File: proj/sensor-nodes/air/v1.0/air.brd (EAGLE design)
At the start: 73 parts, among them J1 54602-908LF, J2 54602-908LF, U2 PCA9615DPJ, U3 MIC4680YM-TR, U4 LM2937IMP3.3NOPB, U5 SHT25, U6 CCS811, U7 T6713-5K, U8 HPP845E034R5

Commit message: minor changes to air sensor node after design review
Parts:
- removed L2: 68uH, openag-inductors:UP2B
- removed SJ4: (no value), openag-connectors:SOLDERJUMPER_REFLOW_NOPASTE
- removed TP10, TP11, TP12, TP31: TPTP06R, openag-testpads:TP06R
- added L1: 68uH, openag-inductors:UP2B
- added SJ2: (no value), openag-connectors:SOLDERJUMPER_REFLOW_NOPASTE
- added TP5, TP6, TP7: TPTP06R, openag-testpads:TP06R
- C4: device openag-capacitors:CT7343 -> openag-capacitors:C0805
- D4: value B260A-13-F -> SBR2A40P1-7; device openag-diodes:SMA -> openag-diodes:POWERDI123
- moved FRAME1 24.1 mm to (77.2, 3.30), turned to 0 degrees
- moved C2\1 22.9 mm to (107.2, 36.1)
- moved C8 22.9 mm to (110.7, 43.1)
- moved R18 22.9 mm to (105.3, 43.1)
- moved TP13 22.9 mm to (111.3, 33.5)
- moved TP14 22.9 mm to (110.0, 33.5)
- moved TP15 22.9 mm to (105.4, 45.0)
- moved TP16 22.9 mm to (103.4, 33.5)
- moved U6 22.9 mm to (109.2, 39.4)
- moved TP24 19.0 mm to (86.6, 45.0), turned to 90 degrees
- moved TP17 17.7 mm to (79.2, 35.1), turned to 90 degrees
- moved TP18 16.8 mm to (78.2, 34.8), turned to 90 degrees
- moved TP23 16.0 mm to (84.6, 36.1), turned to 90 degrees
- moved C10 15.0 mm to (88.9, 42.9), turned to 0 degrees
- moved TP20 13.0 mm to (74.2, 34.8), turned to 90 degrees
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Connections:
- removed net TAB: U4.4
- net +24V: now also C4.1, TP7.TP; no longer C4.+, TP12.TP
- net +5V: now also SJ2.2, TP5.TP; no longer SJ4.2, TP10.TP
- net GND: now also C4.2, D4.-, TP6.TP, U4.4; no longer C4.-, D4.2, TP11.TP, TP31.TP
- net N$31: now also D4.+, L1.1; no longer D4.1, L2.1
- net N$33: now also L1.2, SJ2.1; no longer L2.2, SJ4.1
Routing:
- net +3V3: track 343.5 -> 361.8 mm, vias 2 -> 4
- net N$33: track 25.9 -> 10.7 mm, vias 0 -> 2
- net N$31: track 27.3 -> 16.2 mm, vias 0 -> 2
- net SDA: track 130.4 -> 138.5 mm
- net SCL: track 131.4 -> 137.6 mm, vias 6 -> 4
- net +5V: track 162.2 -> 163.7 mm
- net +24V: track 50.5 -> 51.1 mm
- net GND: vias 9 -> 41
- added copper zone on layer 1, net N$31
- added copper zone on layer 16, net N$31
- added copper zone on layer 1, net N$33
- added copper zone on layer 16, net N$33
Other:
- board outline added: 116.8 x 54.6 mm
- board text added: "24V-to-5V@1A Switching Regulator w/Indicator LED + Enable"
- board text added: "NC"
- board text removed: "24V to 5V@1A Switching Regulator w/Indicator LED + Enable"

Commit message: added light and rj12 nodes, started working on light controller v2
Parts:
- R13, R15, R16, R17: value NV -> 600
- R14, R19: value NV -> 120
- R2, R7: value 100 OHM -> 100
- R20, R21: value NV -> 10K
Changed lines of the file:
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@@
 <setting verticaltext="up"/>
 </settings>
-<grid distance="10" unitdist="mil" unit="mil" style="lines" multiple="1" display="yes" altdistance="5" altunitdist="mil" altunit="mil"/>
+<grid distance="50" unitdist="mil" unit="mil" style="lines" multiple="1" display="yes" altdistance="5" altunitdist="mil" altunit="mil"/>
 <layers>
 <layer number="1" name="Top" color="4" fill="1" visible="yes" active="yes"/>
@@
 <attribute name="VERIFIED" value="NO" x="52.451" y="36.957" size="1.778" layer="27" rot="R180" display="off"/>
 </element>
-<element name="R2" library="openag-resistors" package="RC0603N" value="100 OHM" x="52.451" y="41.148" smashed="yes" rot="R90">
+<element name="R2" library="openag-resistors" package="RC0603N" value="100" x="52.451" y="41.148" smashed="yes" rot="R90">
 <attribute name="NAME" x="51.9557" y="42.4815" size="0.762" layer="25" ratio="6" rot="SR0"/>
 <attribute name="POPULATE" value="YES" x="52.451" y="41.148" size="1.778" layer="27" rot="R90" display="off"/>
@@
 <attribute name="VALUE" value="PCA9615DPJ" x="29.337" y="17.272" size="1.778" layer="27" rot="R270" display="off"/>
 </element>
-<element name="R13" library="openag-resistors" package="RC0603N" value="NV" x="32.639" y="18.288" smashed="yes" rot="R90">
+<element name="R13" library="openag-resistors" package="RC0603N" value="600" x="32.639" y="18.288" smashed="yes" rot="R90">
 <attribute name="NAME" x="34.036" y="17.653" size="0.762" layer="25" rot="R90"/>
-<attribute name="VALUE" value="NV" x="32.004" y="17.653" size="0.762" layer="27" rot="R90"/>
-</element>
-<element name="R14" library="openag-resistors" package="RC0603N" value="NV" x="32.639" y="15.24" smashed="yes" rot="R90">
+<attribute name="VALUE" value="600" x="32.004" y="17.653" size="0.762" layer="27" rot="R90"/>
+</element>
+<element name="R14" library="openag-resistors" package="RC0603N" value="120" x="32.639" y="15.24" smashed="yes" rot="R90">
 <attribute name="NAME" x="34.036" y="14.605" size="0.762" layer="25" rot="R90"/>
-<attribute name="VALUE" value="NV" x="32.004" y="14.605" size="0.762" layer="27" rot="R90"/>
-</element>
-<element name="R15" library="openag-resistors" package="RC0603N" value="NV" x="32.639" y="12.192" smashed="yes" rot="R90">
+<attribute name="VALUE" value="120" x="32.004" y="14.605" size="0.762" layer="27" rot="R90"/>
+</element>
+<element name="R15" library="openag-resistors" package="RC0603N" value="600" x="32.639" y="12.192" smashed="yes" rot="R90">
 <attribute name="NAME" x="34.036" y="11.557" size="0.762" layer="25" rot="R90"/>
-<attribute name="VALUE" value="NV" x="32.004" y="11.557" size="0.762" layer="27" rot="R90"/>
-</element>
-<element name="R16" library="openag-resistors" package="RC0603N" value="NV" x="30.099" y="11.684" smashed="yes">
+<attribute name="VALUE" value="600" x="32.004" y="11.557" size="0.762" layer="27" rot="R90"/>
+</element>
+<element name="R16" library="openag-resistors" package="RC0603N" value="600" x="30.099" y="11.684" smashed="yes">
 <attribute name="NAME" x="30.734" y="11.049" size="0.762" layer="25" rot="R180"/>
-<attribute name="VALUE" value="NV" x="30.734" y="13.081" size="0.762" layer="27" rot="R180"/>
-</element>
-<element name="R17" library="openag-resistors" package="RC0603N" value="NV" x="26.162" y="14.224" smashed="yes" rot="R270">
+<attribute name="VALUE" value="600" x="30.734" y="13.081" size="0.762" layer="27" rot="R180"/>
+</element>
+<element name="R17" library="openag-resistors" package="RC0603N" value="600" x="26.162" y="14.224" smashed="yes" rot="R270">
 <attribute name="NAME" x="25.527" y="13.589" size="0.762" layer="25" rot="R90"/>
-<attribute name="VALUE" value="NV" x="27.559" y="13.589" size="0.762" layer="27" rot="R90"/>
-</element>
-<element name="R19" library="openag-resistors" package="RC0603N" value="NV" x="27.051" y="11.684" smashed="yes">
+<attribute name="VALUE" value="600" x="27.559" y="13.589" size="0.762" layer="27" rot="R90"/>
+</element>
+<element name="R19" library="openag-resistors" package="RC0603N" value="120" x="27.051" y="11.684" smashed="yes">
 <attribute name="NAME" x="27.432" y="11.049" size="0.762" layer="25" rot="R180"/>
-<attribute name="VALUE" value="NV" x="27.686" y="13.081" size="0.762" layer="27" rot="R180"/>
-</element>
-<element name="R20" library="openag-resistors" package="RC0603N" value="NV" x="29.718" y="22.225" smashed="yes">
+<attribute name="VALUE" value="120" x="27.686" y="13.081" size="0.762" layer="27" rot="R180"/>
+</element>
+<element name="R20" library="openag-resistors" package="RC0603N" value="10K" x="29.718" y="22.225" smashed="yes">
 <attribute name="NAME" x="28.448" y="21.717" size="0.762" layer="25" rot="R90"/>
-<attribute name="VALUE" value="NV" x="31.75" y="21.463" size="0.762" layer="27" rot="R90"/>
-</element>
-<element name="R21" library="openag-resistors" package="RC0603N" value="NV" x="29.718" y="25.019" smashed="yes">
+<attribute name="POPULATE" value="YES" x="29.718" y="22.225" size="1.778" layer="27" display="off"/>
+<attribute name="VALUE" value="10K" x="31.75" y="21.463" size="0.762" layer="27" rot="R90"/>
+<attribute name="VERIFIED" value="NO" x="29.718" y="22.225" size="1.778" layer="27" display="off"/>
+</element>
+<element name="R21" library="openag-resistors" package="RC0603N" value="10K" x="29.718" y="25.019" smashed="yes">
 <attribute name="NAME" x="28.448" y="24.257" size="0.762" layer="25" rot="R90"/>
-<attribute name="VALUE" value="NV" x="31.75" y="24.257" size="0.762" layer="27" rot="R90"/>
+<attribute name="POPULATE" value="YES" x="29.718" y="25.019" size="1.778" layer="27" display="off"/>
+<attribute name="VALUE" value="10K" x="31.75" y="24.257" size="0.762" layer="27" rot="R90"/>
+<attribute name="VERIFIED" value="NO" x="29.718" y="25.019" size="1.778" layer="27" display="off"/>
 </element>
 <element name="J2" library="openag_connector" package="OPENAG-V1-RJ45" value="54602-908LF" x="13.97" y="35.56" smashed="yes" rot="R270">
@@
 <attribute name="VALUE" value="976 Ohm" x="48.26" y="24.892" size="0.762" layer="27" ratio="6" rot="R270"/>
 </element>
-<element name="R7" library="openag-resistors" package="RC0603N" value="100 OHM" x="53.213" y="18.288" smashed="yes" rot="R180">
+<element name="R7" library="openag-resistors" package="RC0603N" value="100" x="53.213" y="18.288" smashed="yes" rot="R180">
 <attribute name="NAME" x="52.9082" y="18.9865" size="0.762" layer="25" ratio="6" rot="SR0"/>
 <attribute name="POPULATE" value="YES" x="53.213" y="18.288" size="1.778" layer="27" rot="R180" display="off"/>
-<attribute name="VALUE" x="54.229" y="17.78" size="0.3556" layer="27" ratio="6" rot="R180"/>
+<attribute name="VALUE" value="100" x="54.229" y="17.78" size="0.3556" layer="27" ratio="6" rot="R180"/>
 <attribute name="VERIFIED" value="NO" x="53.213" y="18.288" size="1.778" layer="27" rot="R180" display="off"/>
 </element>

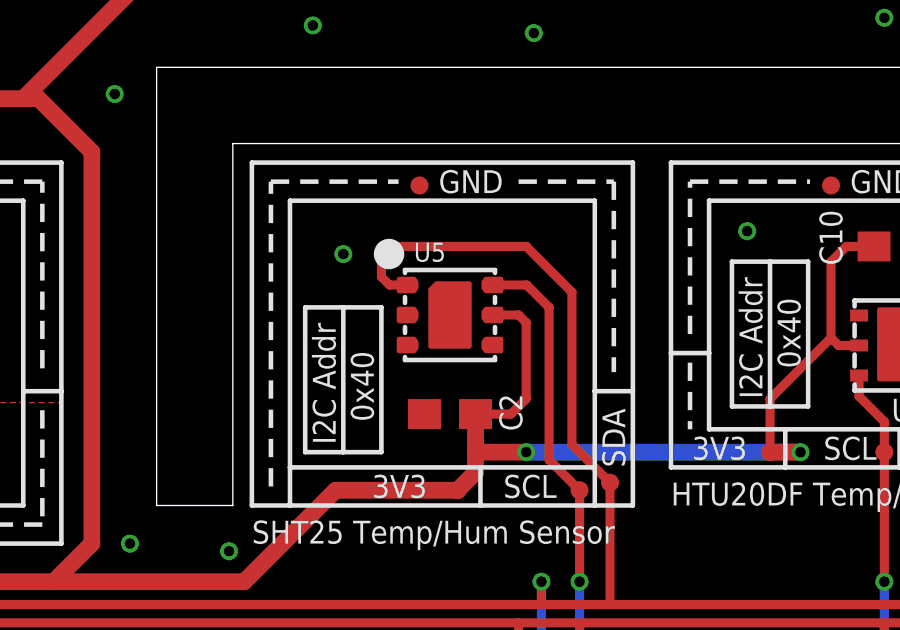
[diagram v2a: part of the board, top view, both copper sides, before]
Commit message: added easy bom generator
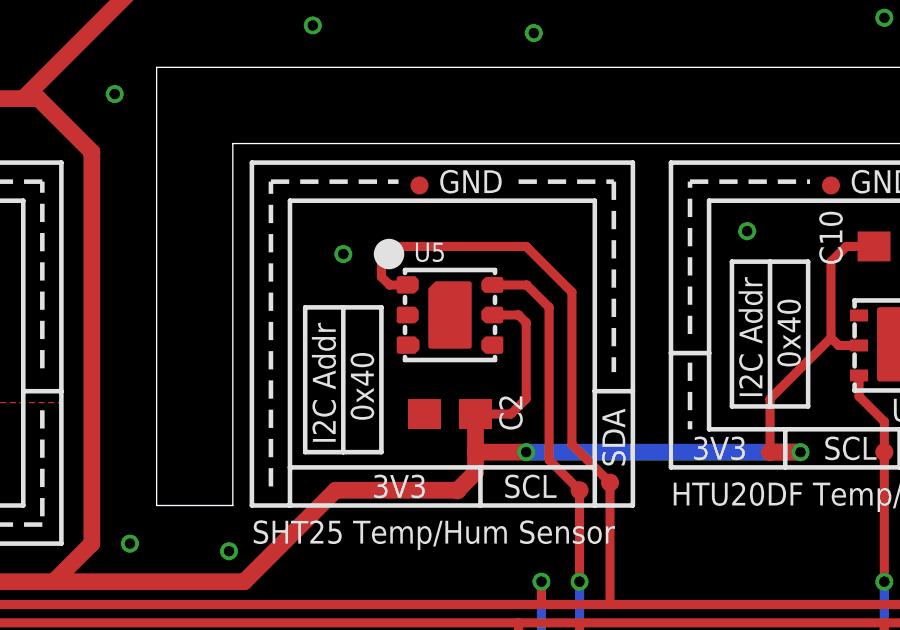
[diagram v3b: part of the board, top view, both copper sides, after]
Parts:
- D1, D5: value APT1608CGCK -> APT1608
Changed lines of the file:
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@@
 <setting verticaltext="up"/>
 </settings>
-<grid distance="50" unitdist="mil" unit="mil" style="lines" multiple="1" display="yes" altdistance="5" altunitdist="mil" altunit="mil"/>
+<grid distance="10" unitdist="mil" unit="mil" style="lines" multiple="1" display="yes" altdistance="5" altunitdist="mil" altunit="mil"/>
 <layers>
 <layer number="1" name="Top" color="4" fill="1" visible="yes" active="yes"/>
@@
 <attribute name="VER" value="1.0" x="77.216" y="3.302" size="1.778" layer="28" rot="MR0" display="off"/>
 </element>
-<element name="D1" library="openag-diodes" package="CHIPLED_0603" value="APT1608CGCK" x="52.451" y="36.957" smashed="yes" rot="R180">
+<element name="D1" library="openag-diodes" package="CHIPLED_0603" value="APT1608" x="52.451" y="36.957" smashed="yes" rot="R180">
 <attribute name="NAME" x="53.086" y="35.56" size="0.762" layer="25" rot="R180"/>
 <attribute name="POPULATE" value="YES" x="52.451" y="36.957" size="1.778" layer="27" rot="R180" display="off"/>
@@
 <attribute name="VERIFIED" value="NO" x="53.213" y="18.288" size="1.778" layer="27" rot="R180" display="off"/>
 </element>
-<element name="D5" library="openag-diodes" package="CHIPLED_0603" value="APT1608CGCK" x="56.0705" y="18.288" smashed="yes" rot="R270">
+<element name="D5" library="openag-diodes" package="CHIPLED_0603" value="APT1608" x="56.0705" y="18.288" smashed="yes" rot="R270">
 <attribute name="NAME" x="56.4515" y="19.685" size="0.762" layer="25" rot="R180"/>
 <attribute name="POPULATE" value="YES" x="56.0705" y="18.288" size="1.778" layer="27" rot="R270" display="off"/>
-<attribute name="VALUE" x="57.0865" y="20.701" size="0.508" layer="27" rot="R180"/>
+<attribute name="VALUE" value="APT1608" x="57.0865" y="20.701" size="0.508" layer="27" rot="R180"/>
 <attribute name="VERIFIED" value="NO" x="56.0705" y="18.288" size="1.778" layer="27" rot="R270" display="off"/>
 </element>
